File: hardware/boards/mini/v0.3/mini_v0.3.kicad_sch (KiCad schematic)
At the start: 97 parts, among them IC1 NAU88C22YG, IC3 IS42S16160J-6BLI, J1 Connector, J2 Top (A), J3 Bottom (B), U1 W25Q128JVP, U2 LTV-217-G, U4 STM32H750XBHx, Y1 Crystal_GND24, Y3 32.768kHz

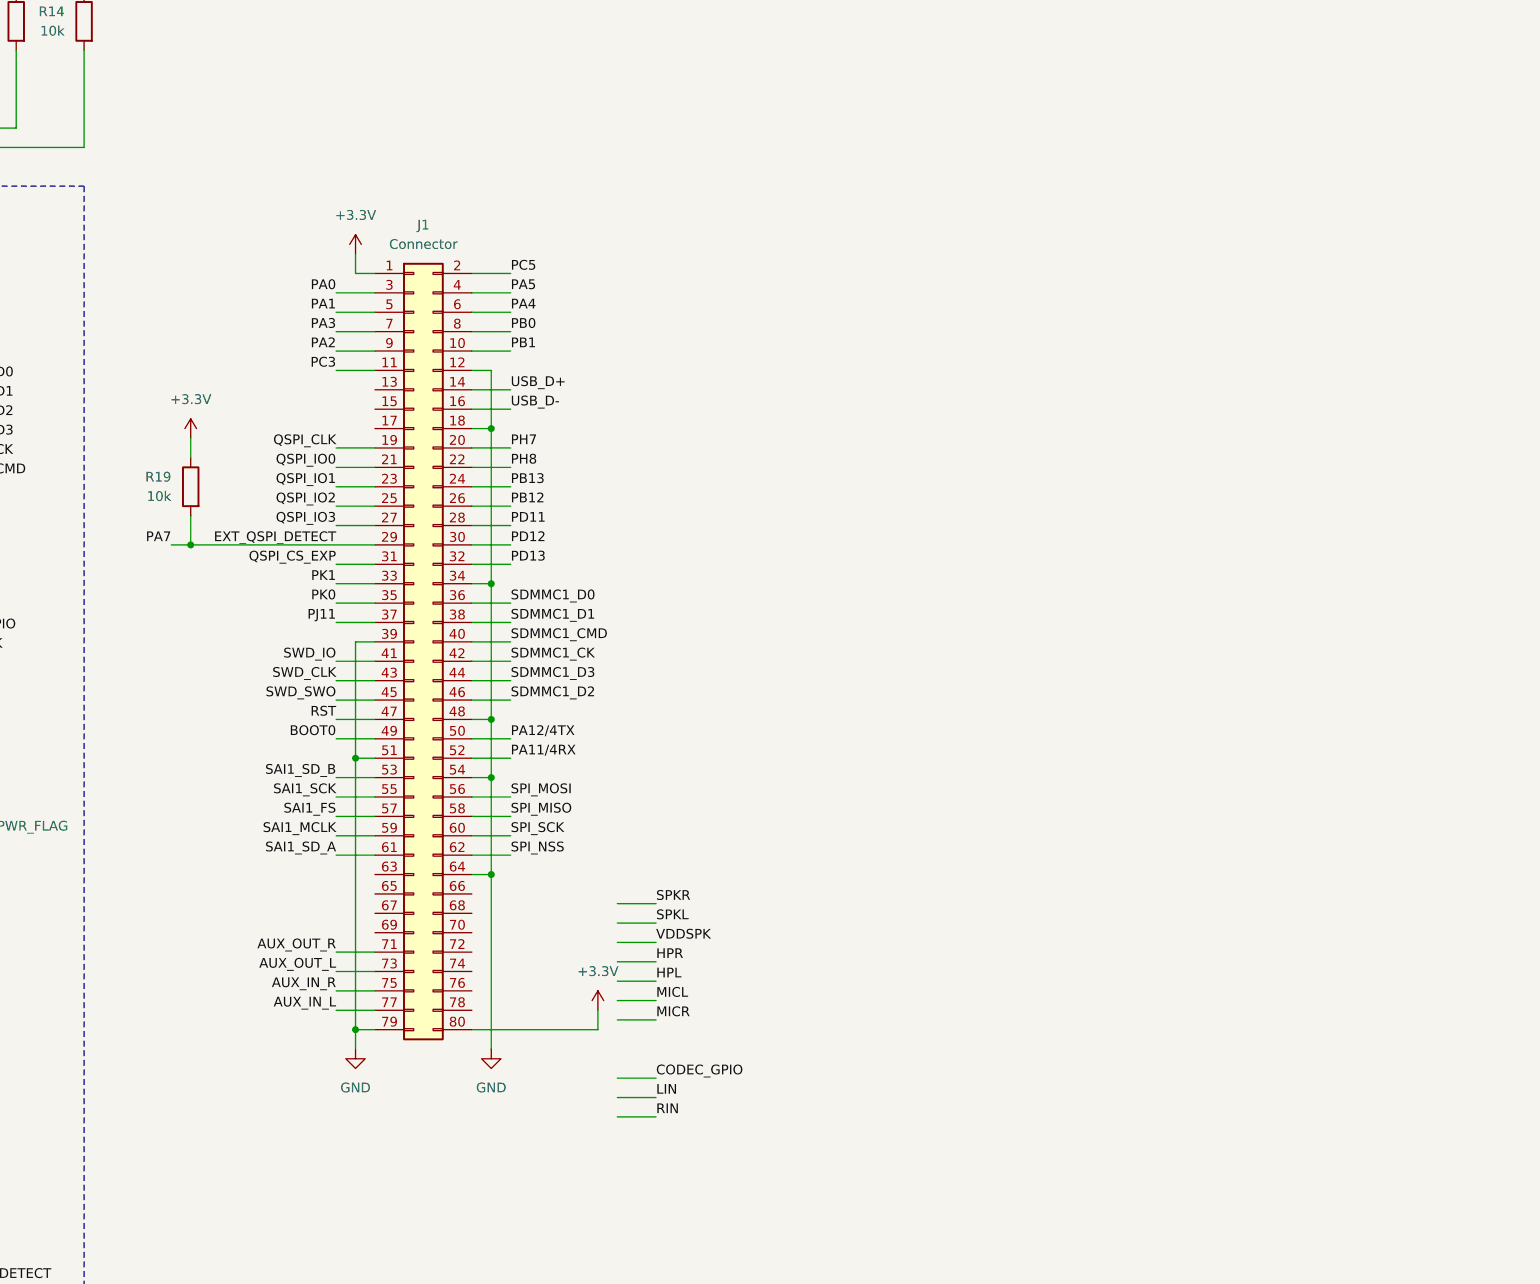
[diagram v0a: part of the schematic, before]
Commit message: mini: use 90-pin port instead of 80
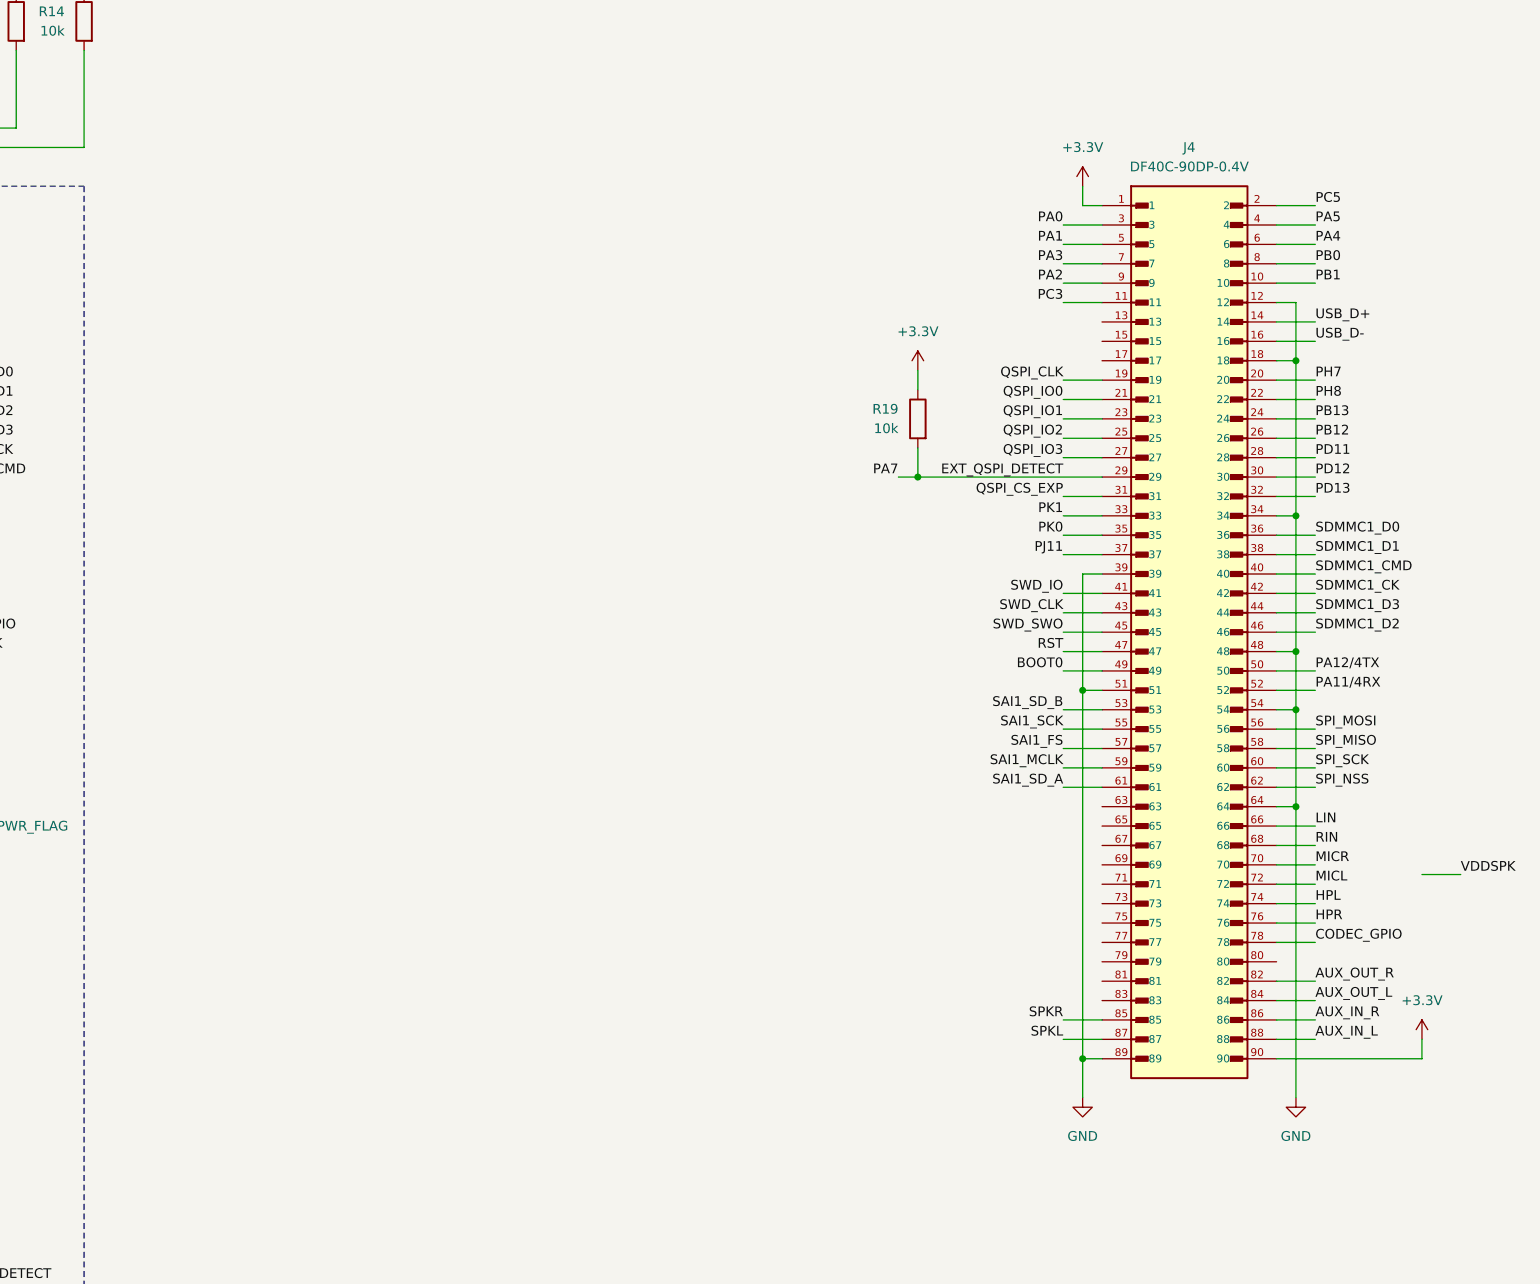
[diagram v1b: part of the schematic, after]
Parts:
- removed J1: Connector, Connector_Hirose_DF40:Hirose_DF40C-80DP-0.4V_2x40-1MP_P0.4mm, symbol Connector_Generic:Conn_02x40_Odd_Even
- added J4: DF40C-90DP-0.4V, Connector_Hirose_DF40:Hirose_DF40C-90DP-0.4V_2x45-1MP_P0.4mm, symbol Rythm:DF40C-90DP-0.4V
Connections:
- net +3.3V: now also J4.1, J4.90
- net AUX_IN_L: now also J4.88
- net AUX_IN_R: now also J4.86
- net AUX_OUT_L: now also J4.84
- net AUX_OUT_R: now also J4.82
- net BOOT0: now also J4.49
- net CODEC_GPIO: now also J4.78
- net EXT_QSPI_DETECT: now also J4.29
- net GND: now also J4.12, J4.18, J4.34, J4.39, J4.48, J4.51, J4.54, J4.64, J4.89
- net HPL: now also J4.74
- net HPR: now also J4.76
- net LIN: now also J4.66
- net MICL: now also J4.72
- net MICR: now also J4.70
- net PA0: now also J4.3
- net PA1: now also J4.5
- net PA11/4RX: now also J4.52
- net PA12/4TX: now also J4.50
- net PA2: now also J4.9
- net PA3: now also J4.7
- net PA4: now also J4.6
- net PA5: now also J4.4
- net PB0: now also J4.8
- net PB1: now also J4.10
- net PB12: now also J4.26
- net PB13: now also J4.24
- net PC3: now also J4.11
- net PC5: now also J4.2
- net PD11: now also J4.28
- net PD12: now also J4.30
- net PD13: now also J4.32
- net PH7: now also J4.20
- net PH8: now also J4.22
- net PJ11: now also J4.37
- net PK0: now also J4.35
- net PK1: now also J4.33
- net QSPI_CLK: now also J4.19
- net QSPI_CS_EXP: now also J4.31
- net QSPI_IO0: now also J4.21
- net QSPI_IO1: now also J4.23
- net QSPI_IO2: now also J4.25
- net QSPI_IO3: now also J4.27
- net RIN: now also J4.68
- net RST: now also J4.47
- net SAI1_FS: now also J4.57
- net SAI1_MCLK: now also J4.59
- net SAI1_SCK: now also J4.55
- net SAI1_SD_A: now also J4.61
- net SAI1_SD_B: now also J4.53
- net SDMMC1_CK: now also J4.42
- net SDMMC1_CMD: now also J4.40
- net SDMMC1_D0: now also J4.36
- net SDMMC1_D1: now also J4.38
- net SDMMC1_D2: now also J4.46
- net SDMMC1_D3: now also J4.44
- net SPI_MISO: now also J4.58
- net SPI_MOSI: now also J4.56
- net SPI_NSS: now also J4.62
- net SPI_SCK: now also J4.60
- net SPKL: now also J4.87
- net SPKR: now also J4.85
- net SWD_CLK: now also J4.43
- net SWD_IO: now also J4.41
- net SWD_SWO: now also J4.45
- net USB_D+: now also J4.14
- net USB_D-: now also J4.16
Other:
- moved on the sheet: R19

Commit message: mini: various routing tweaks
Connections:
- net DIN_IN_SINK: now also J4.81
- net DIN_IN_SOURCE: now also J4.79
- net DIN_OUT_SINK: now also J4.77
- net DIN_OUT_SOURCE: now also J4.75
- net EXT_QSPI_DETECT: no longer J3.37, U4.H15 (PG3)
- net GND: now also J4.63, J4.69, J4.73, J4.83
- net I2C_SCL: now also J4.65
- net I2C_SDA: now also J4.67
- net LED_STATUS2: no longer U4.E2 (PI9)
- net SAI1_MCLK: now also J4.61; no longer J4.59
- net SAI1_SD_A: now also J4.59; no longer J4.61
- new net PA7: J3.37
- no-connect marks 75 -> 76
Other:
- moved on the sheet: J4, R19

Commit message: mini: various routing adjustments
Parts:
- removed D1: POWER, LED_SMD:LED_0402_1005Metric, symbol Device:LED
- removed R16: R, Resistor_SMD:R_0402_1005Metric, symbol Device:R
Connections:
- net DIN_OUT_SINK: now also J4.75; no longer J4.77
- net DIN_OUT_SOURCE: now also J4.77; no longer J4.75
- net EXT_QSPI_DETECT: no longer J4.29, R19.2
- net GND: now also J4.17
- net PC2_C: now also J4.29, R19.2
- net QSPI_IO0: now also J4.27; no longer J4.21
- net QSPI_IO1: now also J4.25; no longer J4.23
- net QSPI_IO2: now also J4.23; no longer J4.25
- net QSPI_IO3: now also J4.21; no longer J4.27
- net VBAT: now also J4.71
